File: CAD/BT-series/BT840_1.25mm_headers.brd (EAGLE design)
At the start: 33.4 x 25.1 mm, 64 parts, among them J1 SM02B-SRSS-TB(LF)(SN), U1 TPD4S012DRYR, U2 BT840, U3 LP5907MFX-3.3/NOPB, U4 LP5907MFX-3.3/NOPB, U5 ADS131M08IPBS, U6 BQ24072RGTR, U7 DX4R005JJ2R1800, X1 ABM3B-8.000MHZ-B2-T, X2 FC-12M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

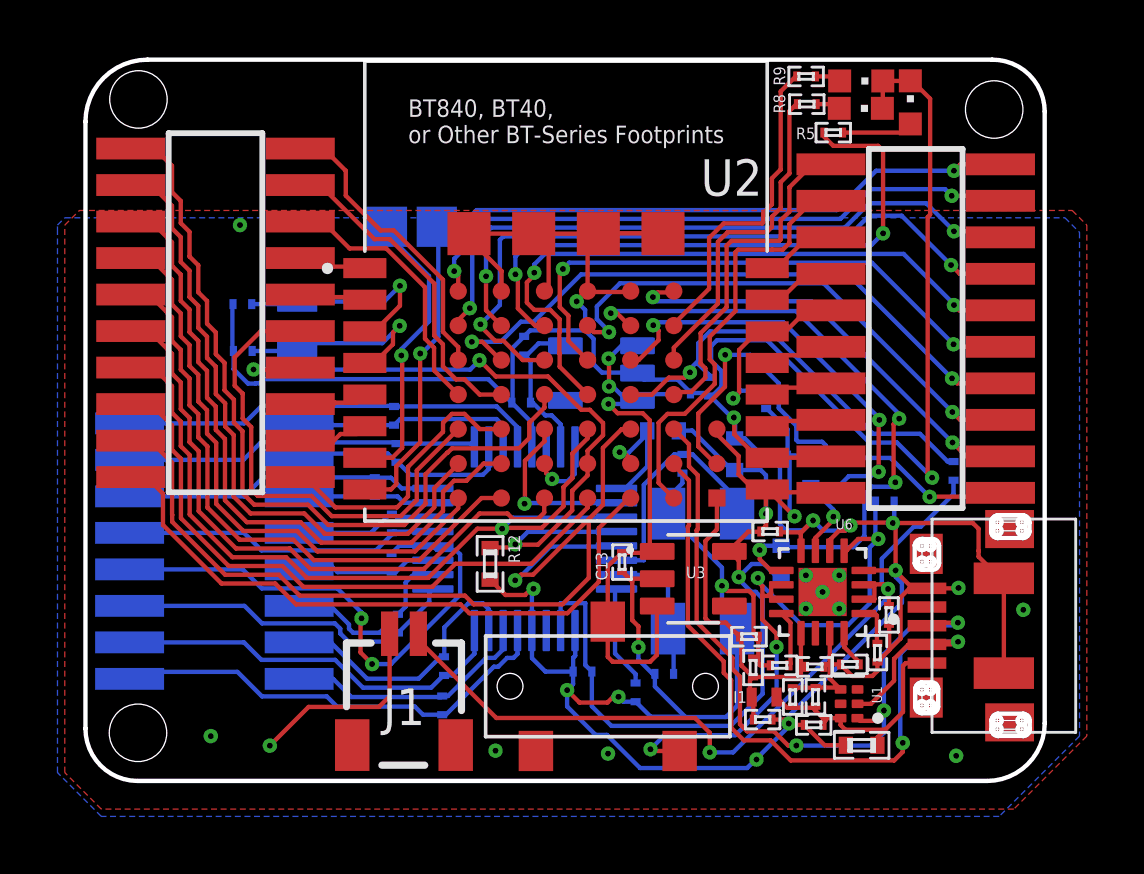
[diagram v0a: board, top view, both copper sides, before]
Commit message: fixed CLKOUT GPIO pin missing, replaced P105 breakout
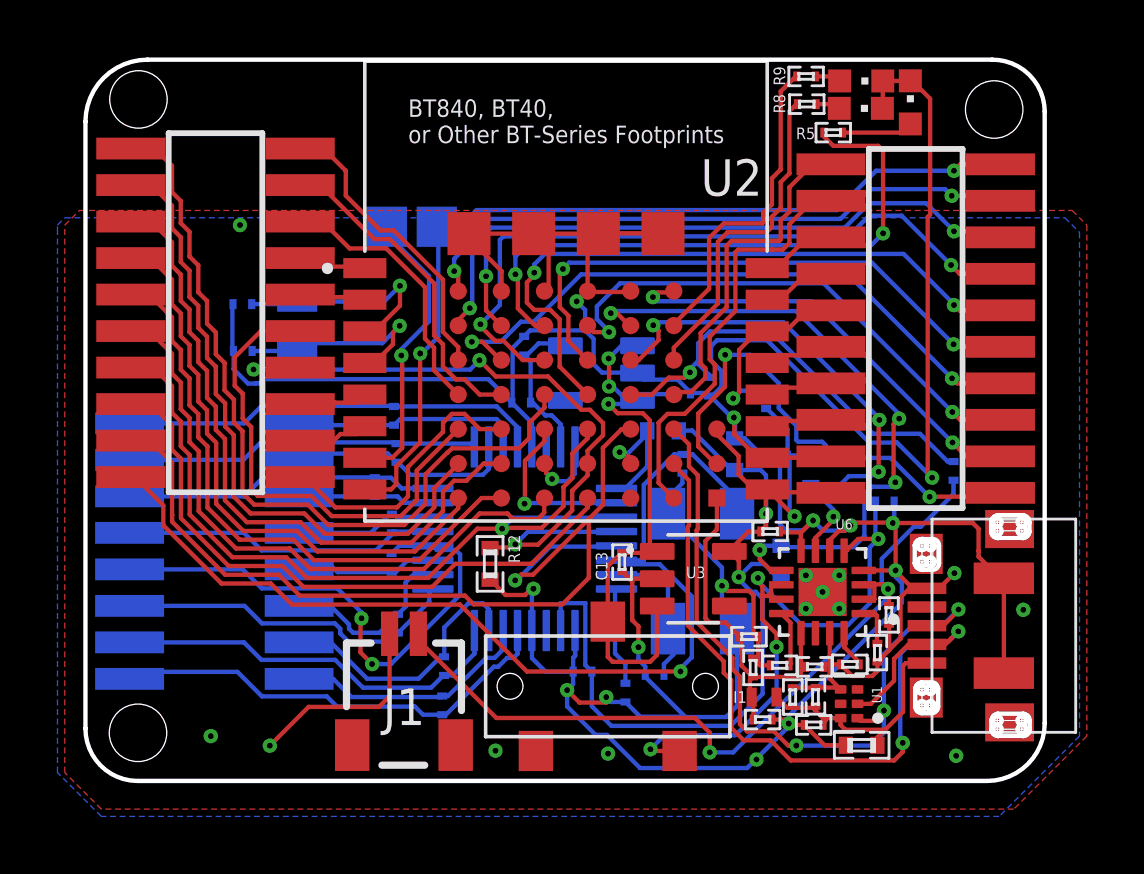
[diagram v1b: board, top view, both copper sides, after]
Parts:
- moved C6 0.35 mm to (26.1, 44.9)
- moved C3 0.34 mm to (27.1, 45.6)
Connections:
- net CLKOUT: now also X3.19
- net P105: no longer X3.19
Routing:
- net CLKOUT: track 8.41 -> 37.2 mm, vias 0 -> 1
- net P105: track 22.8 -> 0.06 mm
